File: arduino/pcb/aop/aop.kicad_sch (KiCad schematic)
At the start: 11 parts, among them J1 Conn_01x02_Pin, M1 RFID-RC522, Q1 AO4435, SW1 SW_Push, SW2 SW_Push, U1 ESP32-C3_SUPERMINI_TH

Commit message: [pcb] AOP v0.1
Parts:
- D1: footprint LED_THT:LED_D3.0mm -> LED_SMD:LED_1206_3216Metric
- M1: footprint RFID-RC522 -> RFID-RC522:RFID-RC522_1
- R1, R2, R3: footprint Resistor_THT:R_Axial_DIN0207_L6.3mm_D2.5mm_P10.16mm_Horizontal -> Resistor_SMD:R_1206_3216Metric
- SW1: footprint Resistor_THT:R_Axial_DIN0414_L11.9mm_D4.5mm_P15.24mm_Horizontal -> Resistor_THT:R_Axial_DIN0207_L6.3mm_D2.5mm_P5.08mm_Vertical
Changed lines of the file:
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@@
+	(wire
+		(pts
+			(xy 59.69 82.55) (xy 74.93 82.55)
+		)
+		(stroke
+			(width 0)
+			(type default)
+		)
+	)
 	(wire
 		(pts
@@
 		(pts
 			(xy 90.17 110.49) (xy 74.93 110.49)
-		)
-		(stroke
-			(width 0)
-			(type default)
-		)
-	)
-	(wire
-		(pts
-			(xy 59.69 82.55) (xy 74.93 82.55)
 		)
 		(stroke
@@
 			)
 		)
-		(property "Footprint" "Resistor_THT:R_Axial_DIN0207_L6.3mm_D2.5mm_P10.16mm_Horizontal"
+		(property "Footprint" "Resistor_SMD:R_1206_3216Metric"
 			(at 38.608 82.55 90)
 			(effects
@@
 		)
 		(instances
-			(project ""
+			(project "aop"
 				(path "/6c2f9cd3-2815-4cb2-b88c-9d452fcffe7c"
 					(reference "R3")
@@
 		)
 		(instances
-			(project ""
+			(project "aop"
 				(path "/6c2f9cd3-2815-4cb2-b88c-9d452fcffe7c"
 					(reference "#PWR011")
@@
 		)
 		(instances
-			(project ""
+			(project "aop"
 				(path "/6c2f9cd3-2815-4cb2-b88c-9d452fcffe7c"
 					(reference "#PWR03")
@@
 		)
 		(instances
-			(project ""
+			(project "aop"
 				(path "/6c2f9cd3-2815-4cb2-b88c-9d452fcffe7c"
 					(reference "U1")
@@
 			)
 		)
-		(property "Footprint" "Resistor_THT:R_Axial_DIN0207_L6.3mm_D2.5mm_P10.16mm_Horizontal"
+		(property "Footprint" "Resistor_SMD:R_1206_3216Metric"
 			(at 123.952 91.44 90)
 			(effects
@@
 		)
 		(instances
-			(project ""
+			(project "aop"
 				(path "/6c2f9cd3-2815-4cb2-b88c-9d452fcffe7c"
 					(reference "R2")
@@
 		)
 		(instances
-			(project ""
+			(project "aop"
 				(path "/6c2f9cd3-2815-4cb2-b88c-9d452fcffe7c"
 					(reference "#PWR08")
@@
 		)
 		(instances
-			(project ""
+			(project "aop"
 				(path "/6c2f9cd3-2815-4cb2-b88c-9d452fcffe7c"
 					(reference "BZ1")
@@
 			)
 		)
-		(property "Footprint" "Resistor_THT:R_Axial_DIN0414_L11.9mm_D4.5mm_P15.24mm_Horizontal"
+		(property "Footprint" "Resistor_THT:R_Axial_DIN0207_L6.3mm_D2.5mm_P5.08mm_Vertical"
 			(at 54.61 67.31 0)
 			(effects
@@
 		)
 		(instances
-			(project ""
+			(project "aop"
 				(path "/6c2f9cd3-2815-4cb2-b88c-9d452fcffe7c"
 					(reference "SW1")
@@
 		)
 		(instances
-			(project ""
+			(project "aop"
 				(path "/6c2f9cd3-2815-4cb2-b88c-9d452fcffe7c"
 					(reference "#PWR01")
@@
 		)
 		(instances
-			(project ""
+			(project "aop"
 				(path "/6c2f9cd3-2815-4cb2-b88c-9d452fcffe7c"
 					(reference "#PWR09")
@@
 		)
 		(instances
-			(project ""
+			(project "aop"
 				(path "/6c2f9cd3-2815-4cb2-b88c-9d452fcffe7c"
 					(reference "J1")
@@
 		)
 		(instances
-			(project ""
+			(project "aop"
 				(path "/6c2f9cd3-2815-4cb2-b88c-9d452fcffe7c"
 					(reference "#PWR05")
@@
 		)
 		(instances
-			(project ""
+			(project "aop"
 				(path "/6c2f9cd3-2815-4cb2-b88c-9d452fcffe7c"
 					(reference "Q1")
@@
 		)
 		(instances
-			(project ""
+			(project "aop"
 				(path "/6c2f9cd3-2815-4cb2-b88c-9d452fcffe7c"
 					(reference "#PWR012")
@@
 			)
 		)
-		(property "Footprint" "RFID-RC522"
+		(property "Footprint" "RFID-RC522:RFID-RC522_1"
 			(at 143.51 120.65 0)
 			(effects
@@
 		)
 		(instances
-			(project ""
+			(project "aop"
 				(path "/6c2f9cd3-2815-4cb2-b88c-9d452fcffe7c"
 					(reference "M1")
@@
 			)
 		)
-		(property "Footprint" "LED_THT:LED_D3.0mm"
+		(property "Footprint" "LED_SMD:LED_1206_3216Metric"
 			(at 36.83 74.93 0)
 			(effects
@@
 		)
 		(instances
-			(project ""
+			(project "aop"
 				(path "/6c2f9cd3-2815-4cb2-b88c-9d452fcffe7c"
 					(reference "D1")
@@
 		)
 		(instances
-			(project ""
+			(project "aop"
 				(path "/6c2f9cd3-2815-4cb2-b88c-9d452fcffe7c"
 					(reference "#PWR04")
@@
 		)
 		(instances
-			(project ""
+			(project "aop"
 				(path "/6c2f9cd3-2815-4cb2-b88c-9d452fcffe7c"
 					(reference "#PWR07")
@@
 		)
 		(instances
-			(project ""
+			(project "aop"
 				(path "/6c2f9cd3-2815-4cb2-b88c-9d452fcffe7c"
 					(reference "#PWR010")
@@
 			)
 		)
-		(property "Footprint" "Resistor_THT:R_Axial_DIN0207_L6.3mm_D2.5mm_P10.16mm_Horizontal"
+		(property "Footprint" "Resistor_SMD:R_1206_3216Metric"
 			(at 119.38 73.152 90)
 			(effects
@@
 		)
 		(instances
-			(project ""
+			(project "aop"
 				(path "/6c2f9cd3-2815-4cb2-b88c-9d452fcffe7c"
 					(reference "R1")

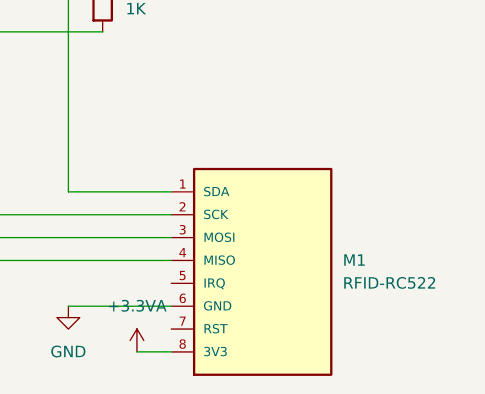
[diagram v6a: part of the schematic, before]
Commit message: [pcb] Increase the length
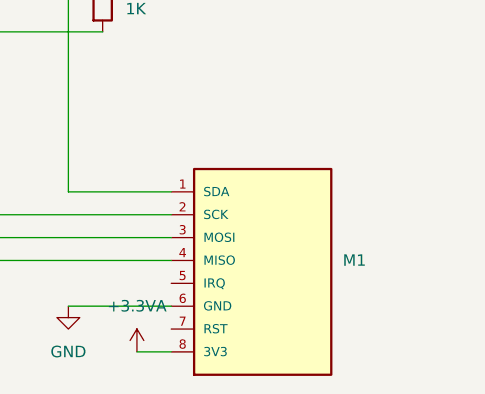
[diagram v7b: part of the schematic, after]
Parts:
- M1: value RFID-RC522 -> (none)

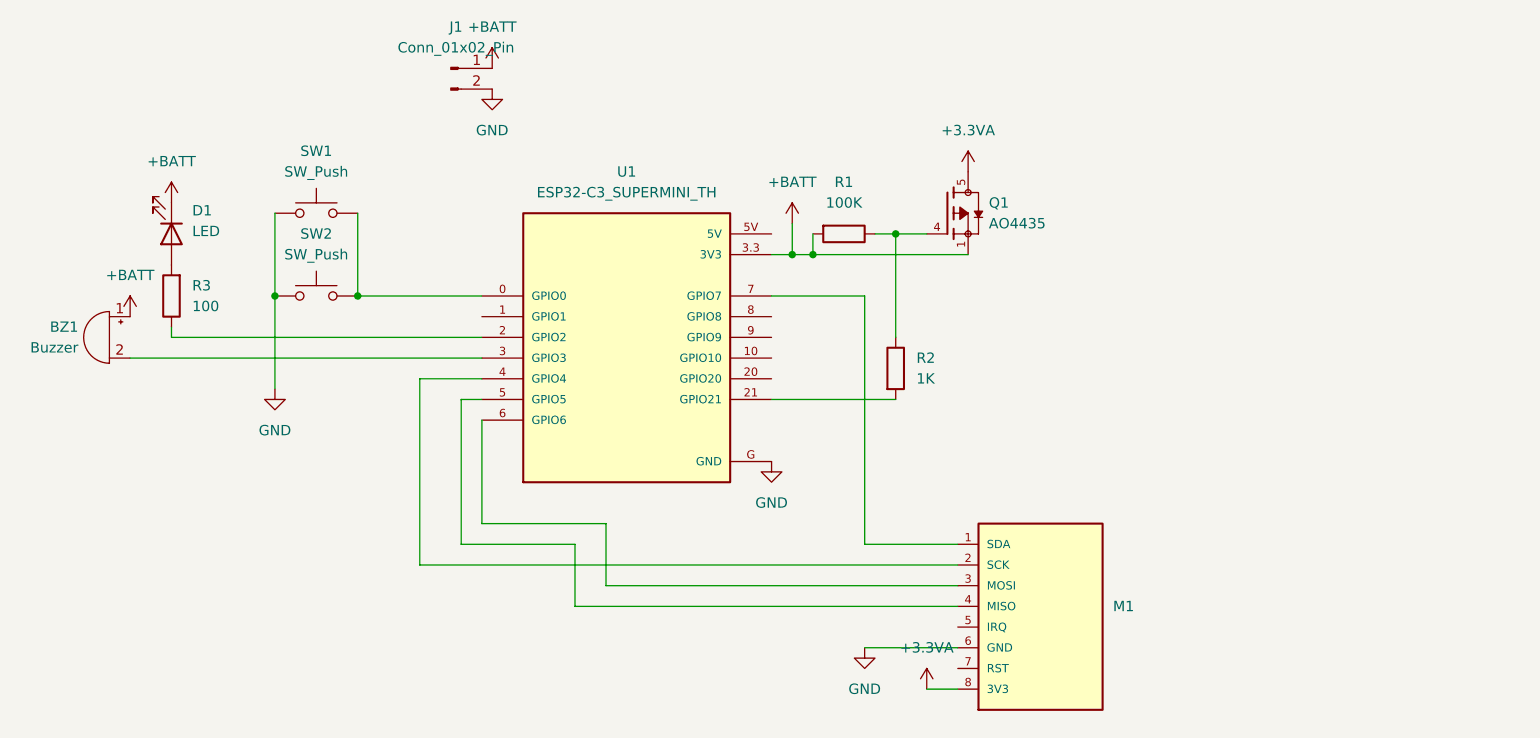
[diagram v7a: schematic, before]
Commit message: [pcb] Prepare 0.2 for fabrication
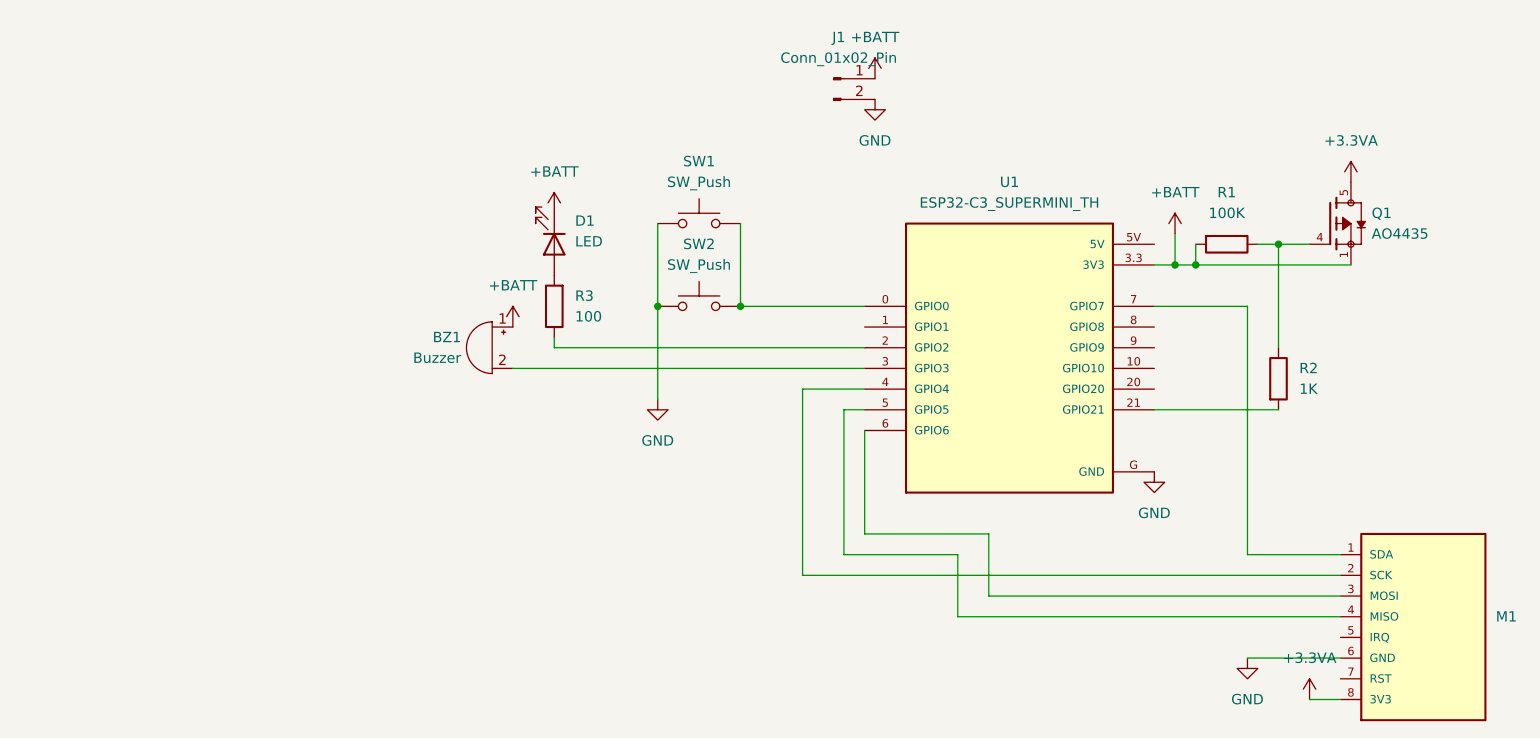
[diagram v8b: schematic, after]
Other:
- title: (none) -> AOP
- moved on the sheet: BZ1, D1, J1, M1, Q1, R1, R2, R3, SW1, SW2, U1
